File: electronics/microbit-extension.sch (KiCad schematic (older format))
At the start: 20 parts, among them SW1 SW_DIP_x01, SW2 SW_DIP_x01, SW3 SW_DIP_x01, SW4 SW_DIP_x01

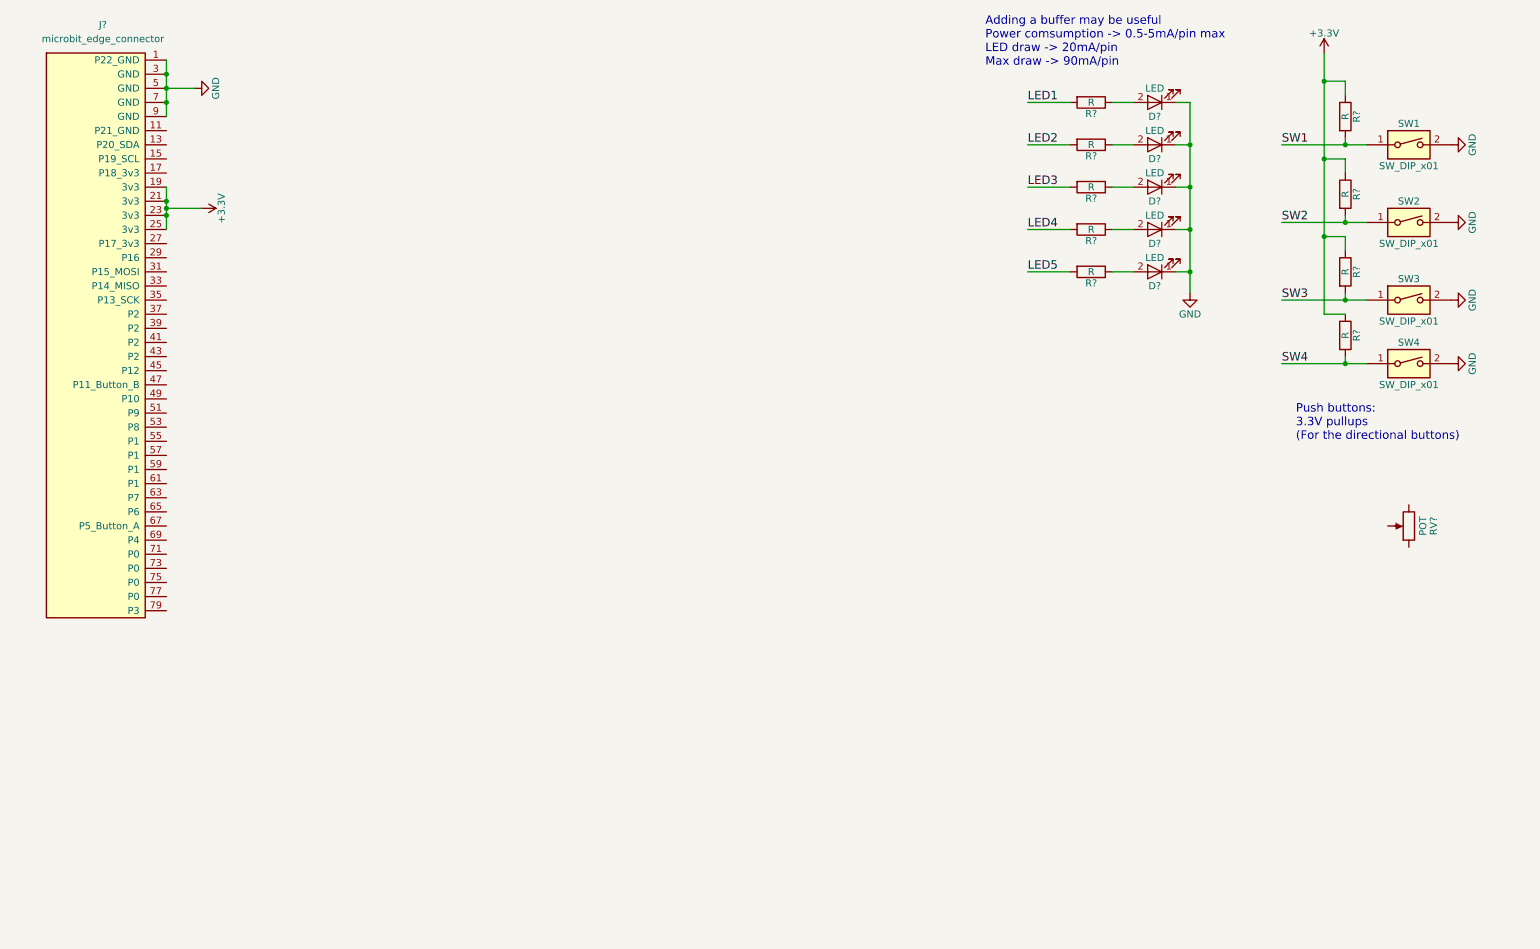
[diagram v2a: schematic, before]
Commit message: added LED buffers
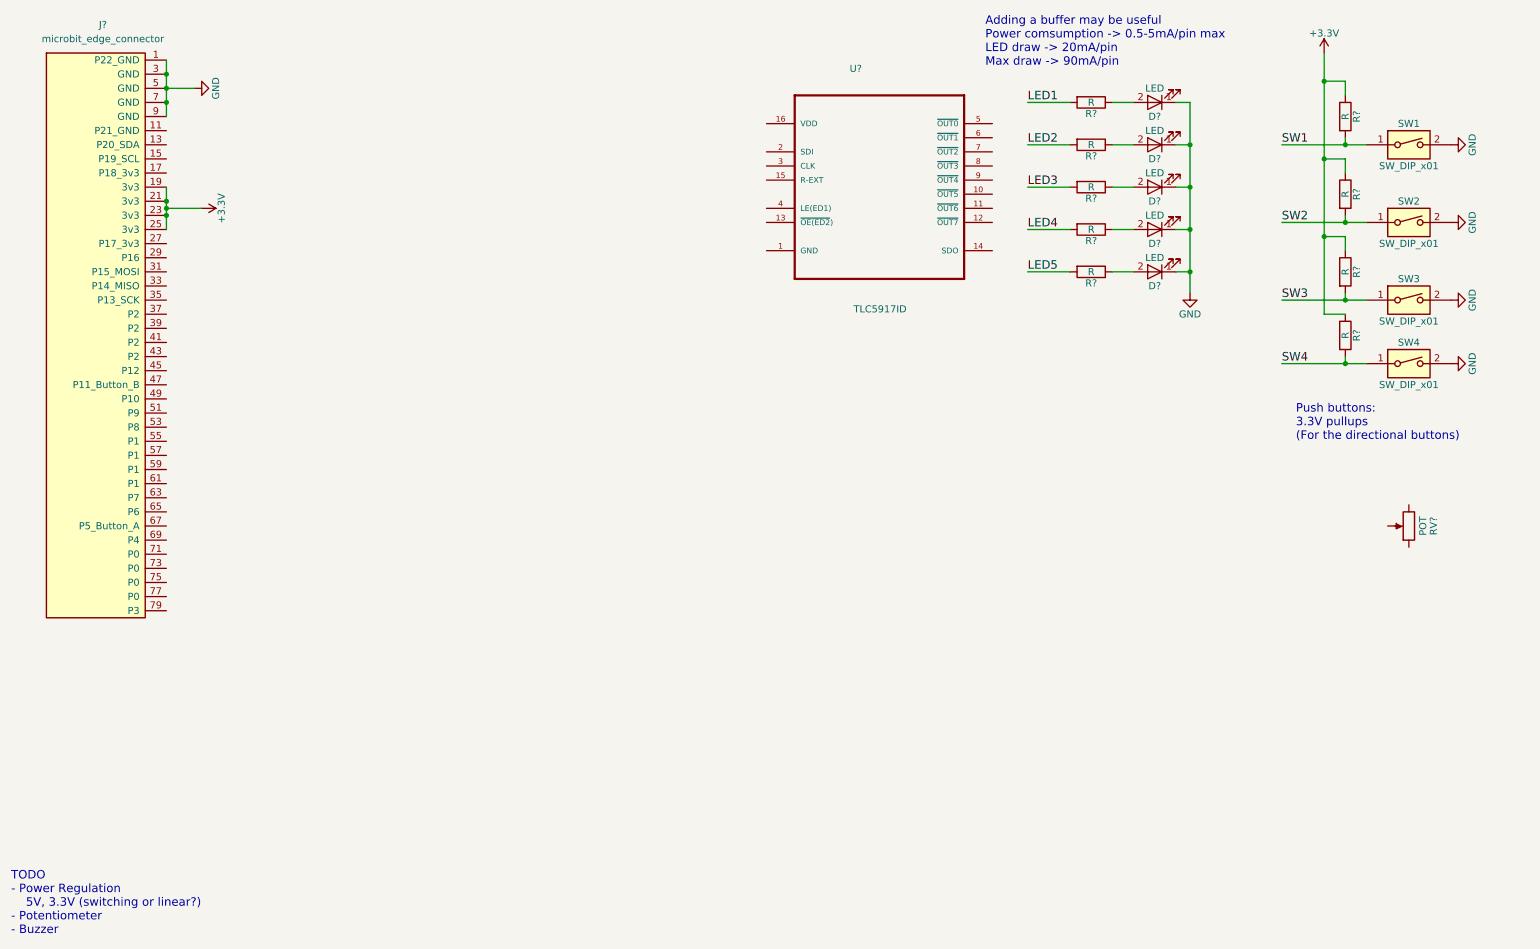
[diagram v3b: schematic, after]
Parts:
- added U?: TLC5917ID, SOIC127P600X175-16N, symbol TLC5917ID
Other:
- note added: "TODO\n- Power Regulation\n 5V, 3.3V (switching or linear?)\n- Potentiometer\n- Buzzer"
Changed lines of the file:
@@
 LIBS:lib_microbit_connector
 LIBS:switches
+LIBS:TLC5917ID
 LIBS:microbit-extension-cache
 EELAYER 25 0
@@
 Text Notes 7600 900  0    60   ~ 0
 Adding a buffer may be useful\nPower comsumption -> 0.5-5mA/pin max\nLED draw -> 20mA/pin\nMax draw -> 90mA/pin\n
+$Comp
+L TLC5917ID U?
+U 1 1 5985BE76
+P 6850 1600
+F 0 "U?" H 6639 2260 50  0000 L BNN
+F 1 "TLC5917ID" H 6667 557 50  0000 L BNN
+F 2 "SOIC127P600X175-16N" H 6850 1600 50  0001 L BNN
+F 3 "1.11 USD" H 6850 1600 50  0001 L BNN
+F 4 "TLC5917IN" H 6850 1600 50  0001 L BNN "MP"
+F 5 "8-Bit Constant-Current LED Sink Driver 16-PDIP -40 to 125" H 6850 1600 50  0001 L BNN "Description"
+F 6 "Good" H 6850 1600 50  0001 L BNN "Availability"
+F 7 "PDIP-16 Texas Instruments" H 6850 1600 50  0001 L BNN "Package"
+F 8 "Texas Instruments" H 6850 1600 50  0001 L BNN "MF"
+	1    6850 1600
+	1    0    0    -1
+$EndComp
+Text Notes 700  7050 0    60   ~ 0
+TODO\n- Power Regulation\n	5V, 3.3V (switching or linear?)\n- Potentiometer\n- Buzzer
 $EndSCHEMATC

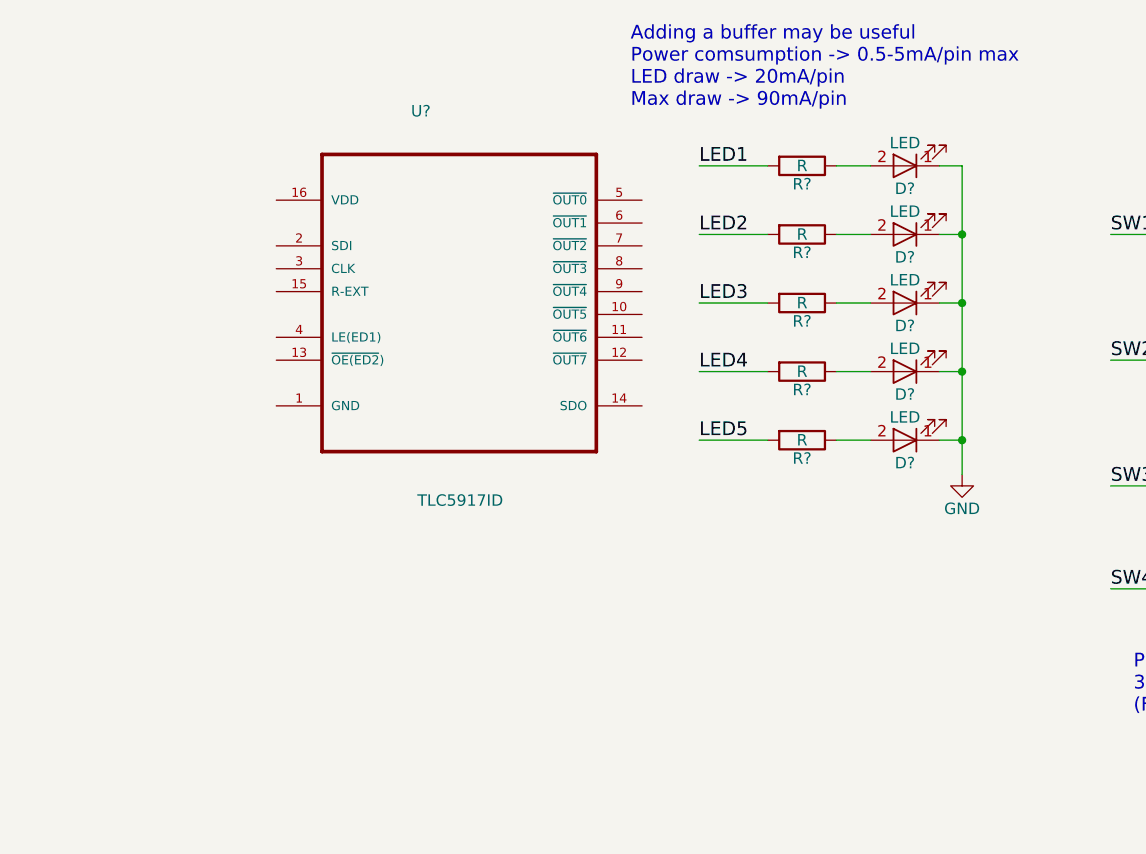
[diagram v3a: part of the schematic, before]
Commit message: added LED driver and RGB LED
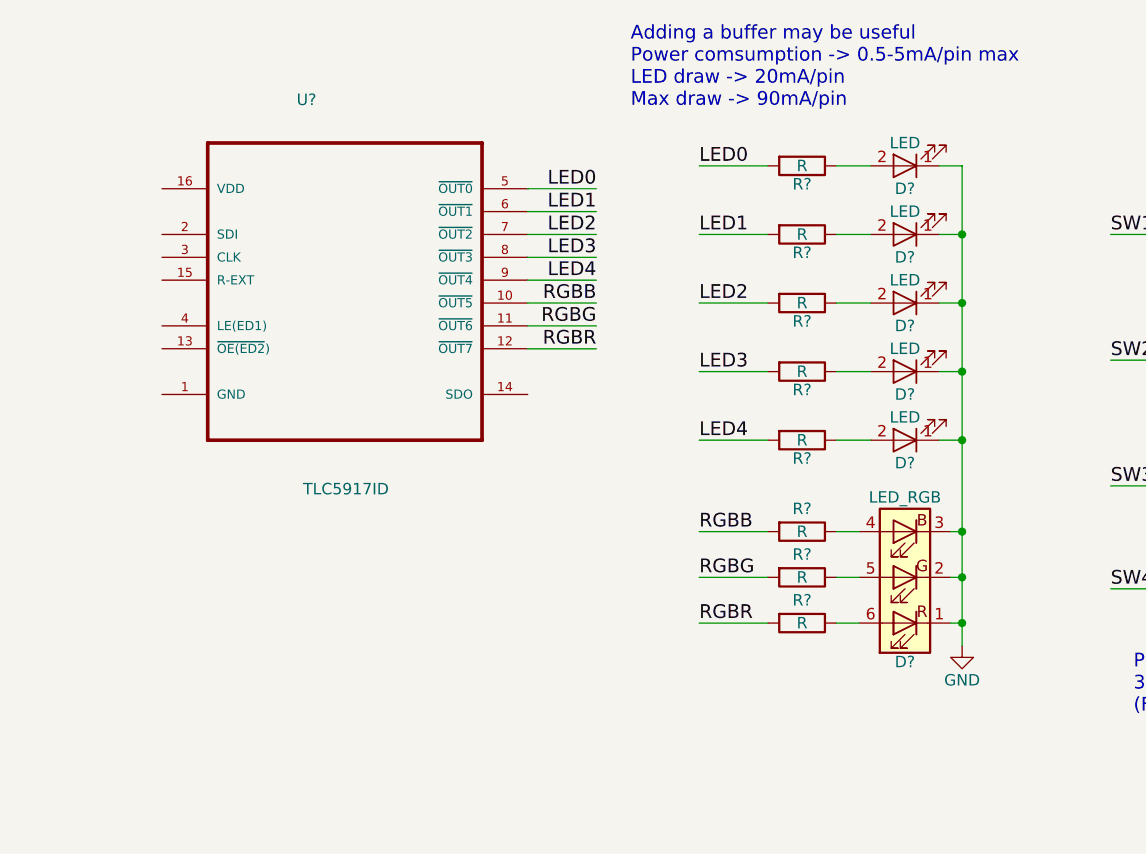
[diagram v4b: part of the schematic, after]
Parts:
- added D?: LED_RGB, symbol LED_RGB
- added R? (x3): R, symbol R
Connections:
- net LED5 is gone; now on net LED4: R?.2
- net GND: now also D?.1 (RK), D?.2 (GK), D?.3 (BK)
- net LED1: now also R?.2, U?.6 (~OUT1); no longer R?.2
- net LED2: now also R?.2, U?.7 (~OUT2); no longer R?.2
- net LED3: now also R?.2, U?.8 (~OUT3); no longer R?.2
- net LED4: now also U?.9 (~OUT4); no longer R?.2
- net RGBB: now reaches U?.10 (~OUT5)
- net RGBB: now also R?.2
- net RGBG: now reaches U?.11 (~OUT6)
- net RGBG: now also R?.2
- net RGBR: now reaches U?.12 (~OUT7)
- net RGBR: now also R?.2
- net LED0: now reaches U?.5 (~OUT0)
- net LED0: now also R?.2
- new net: D?.4 (BA), R?.1
- new net: D?.5 (GA), R?.1
- new net: D?.6 (RA), R?.1
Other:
- moved on the sheet: U?
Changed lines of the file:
@@
 $EndComp
 Text Label 7900 1150 0    60   ~ 0
-LED1
+LED0
 $Comp
 L LED D?
@@
 $EndComp
 Text Label 7900 1750 0    60   ~ 0
-LED3
+LED2
 $Comp
 L LED D?
@@
 $EndComp
 Text Label 7900 1450 0    60   ~ 0
-LED2
+LED1
 $Comp
 L LED D?
@@
 $EndComp
 Text Label 7900 2050 0    60   ~ 0
-LED4
+LED3
 $Comp
 L LED D?
@@
 L GND #PWR?
 U 1 1 59859CA3
-P 9050 2500
-F 0 "#PWR?" H 9050 2250 50  0001 C CNN
-F 1 "GND" H 9050 2350 50  0000 C CNN
-F 2 "" H 9050 2500 50  0001 C CNN
-F 3 "" H 9050 2500 50  0001 C CNN
-	1    9050 2500
+P 9050 3250
+F 0 "#PWR?" H 9050 3000 50  0001 C CNN
+F 1 "GND" H 9050 3100 50  0000 C CNN
+F 2 "" H 9050 3250 50  0001 C CNN
+F 3 "" H 9050 3250 50  0001 C CNN
+	1    9050 3250
 	1    0    0    -1
 $EndComp
 Text Label 7900 2350 0    60   ~ 0
-LED5
+LED4
 $Comp
 L +3.3V #PWR?
@@
 	7900 2350 8200 2350
 Wire Wire Line
-	9050 1150 9050 2500
+	9050 1150 9050 3250
 Connection ~ 9050 1450
 Connection ~ 9050 1750
@@
 L TLC5917ID U?
 U 1 1 5985BE76
-P 6850 1600
-F 0 "U?" H 6639 2260 50  0000 L BNN
-F 1 "TLC5917ID" H 6667 557 50  0000 L BNN
-F 2 "SOIC127P600X175-16N" H 6850 1600 50  0001 L BNN
-F 3 "1.11 USD" H 6850 1600 50  0001 L BNN
-F 4 "TLC5917IN" H 6850 1600 50  0001 L BNN "MP"
-F 5 "8-Bit Constant-Current LED Sink Driver 16-PDIP -40 to 125" H 6850 1600 50  0001 L BNN "Description"
-F 6 "Good" H 6850 1600 50  0001 L BNN "Availability"
-F 7 "PDIP-16 Texas Instruments" H 6850 1600 50  0001 L BNN "Package"
-F 8 "Texas Instruments" H 6850 1600 50  0001 L BNN "MF"
-	1    6850 1600
+P 6350 1550
+F 0 "U?" H 6139 2210 50  0000 L BNN
+F 1 "TLC5917ID" H 6167 507 50  0000 L BNN
+F 2 "SOIC127P600X175-16N" H 6350 1550 50  0001 L BNN
+F 3 "1.11 USD" H 6350 1550 50  0001 L BNN
+F 4 "TLC5917IN" H 6350 1550 50  0001 L BNN "MP"
+F 5 "8-Bit Constant-Current LED Sink Driver 16-PDIP -40 to 125" H 6350 1550 50  0001 L BNN "Description"
+F 6 "Good" H 6350 1550 50  0001 L BNN "Availability"
+F 7 "PDIP-16 Texas Instruments" H 6350 1550 50  0001 L BNN "Package"
+F 8 "Texas Instruments" H 6350 1550 50  0001 L BNN "MF"
+	1    6350 1550
 	1    0    0    -1
 $EndComp
 Text Notes 700  7050 0    60   ~ 0
 TODO\n- Power Regulation\n	5V, 3.3V (switching or linear?)\n- Potentiometer\n- Buzzer
+Text Label 7450 1250 2    60   ~ 0
+LED0
+Text Label 7450 1350 2    60   ~ 0
+LED1
+Text Label 7450 1450 2    60   ~ 0
+LED2
+Text Label 7450 1550 2    60   ~ 0
+LED3
+Text Label 7450 1650 2    60   ~ 0
+LED4
+Wire Wire Line
+	7150 1250 7450 1250
+Wire Wire Line
+	7150 1350 7450 1350
+Wire Wire Line
+	7150 1450 7450 1450
+Wire Wire Line
+	7150 1550 7450 1550
+Wire Wire Line
+	7150 1650 7450 1650
+$Comp
+L LED_RGB D?
+U 1 1 598674A3
+P 8800 2950
+F 0 "D?" H 8800 3320 50  0000 C CNN
+F 1 "LED_RGB" H 8800 2600 50  0000 C CNN
+F 2 "" H 8800 2900 50  0001 C CNN
+F 3 "" H 8800 2900 50  0001 C CNN
+	1    8800 2950
+	-1   0    0    1
+$EndComp
+Wire Wire Line
+	9000 2750 9050 2750
+Connection ~ 9050 2750
+Wire Wire Line
+	9000 2950 9050 2950
+Connection ~ 9050 2950
+Wire Wire Line
+	9000 3150 9050 3150
+Connection ~ 9050 3150
+$Comp
+L R R?
+U 1 1 598678F8
+P 8350 2750
+F 0 "R?" V 8250 2750 50  0000 C CNN
+F 1 "R" V 8350 2750 50  0000 C CNN
+F 2 "" V 8280 2750 50  0001 C CNN
+F 3 "" H 8350 2750 50  0001 C CNN
+	1    8350 2750
+	0    1    1    0
+$EndComp
+Text Label 7900 2750 0    60   ~ 0
+RGBB
+$Comp
+L R R?
+U 1 1 598678FF
+P 8350 2950
+F 0 "R?" V 8250 2950 50  0000 C CNN
+F 1 "R" V 8350 2950 50  0000 C CNN
+F 2 "" V 8280 2950 50  0001 C CNN
+F 3 "" H 8350 2950 50  0001 C CNN
+	1    8350 2950
+	0    1    1    0
+$EndComp
+Text Label 7900 2950 0    60   ~ 0
+RGBG
+$Comp
+L R R?
+U 1 1 59867906
+P 8350 3150
+F 0 "R?" V 8250 3150 50  0000 C CNN
+F 1 "R" V 8350 3150 50  0000 C CNN
+F 2 "" V 8280 3150 50  0001 C CNN
+F 3 "" H 8350 3150 50  0001 C CNN
+	1    8350 3150
+	0    1    1    0
+$EndComp
+Text Label 7900 3150 0    60   ~ 0
+RGBR
+Wire Wire Line
+	7900 2750 8200 2750
+Wire Wire Line
+	7900 2950 8200 2950
+Wire Wire Line
+	7900 3150 8200 3150
+Wire Wire Line
+	8500 2750 8600 2750
+Wire Wire Line
+	8500 2950 8600 2950
+Wire Wire Line
+	8500 3150 8600 3150
+Wire Wire Line
+	7150 1750 7450 1750
+Wire Wire Line
+	7150 1850 7450 1850
+Wire Wire Line
+	7150 1950 7450 1950
+Text Label 7450 1750 2    60   ~ 0
+RGBB
+Text Label 7450 1850 2    60   ~ 0
+RGBG
+Text Label 7450 1950 2    60   ~ 0
+RGBR
 $EndSCHEMATC
